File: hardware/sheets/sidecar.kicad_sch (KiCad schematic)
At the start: 3 parts, among them J1 Conn_02x32_Odd_Even

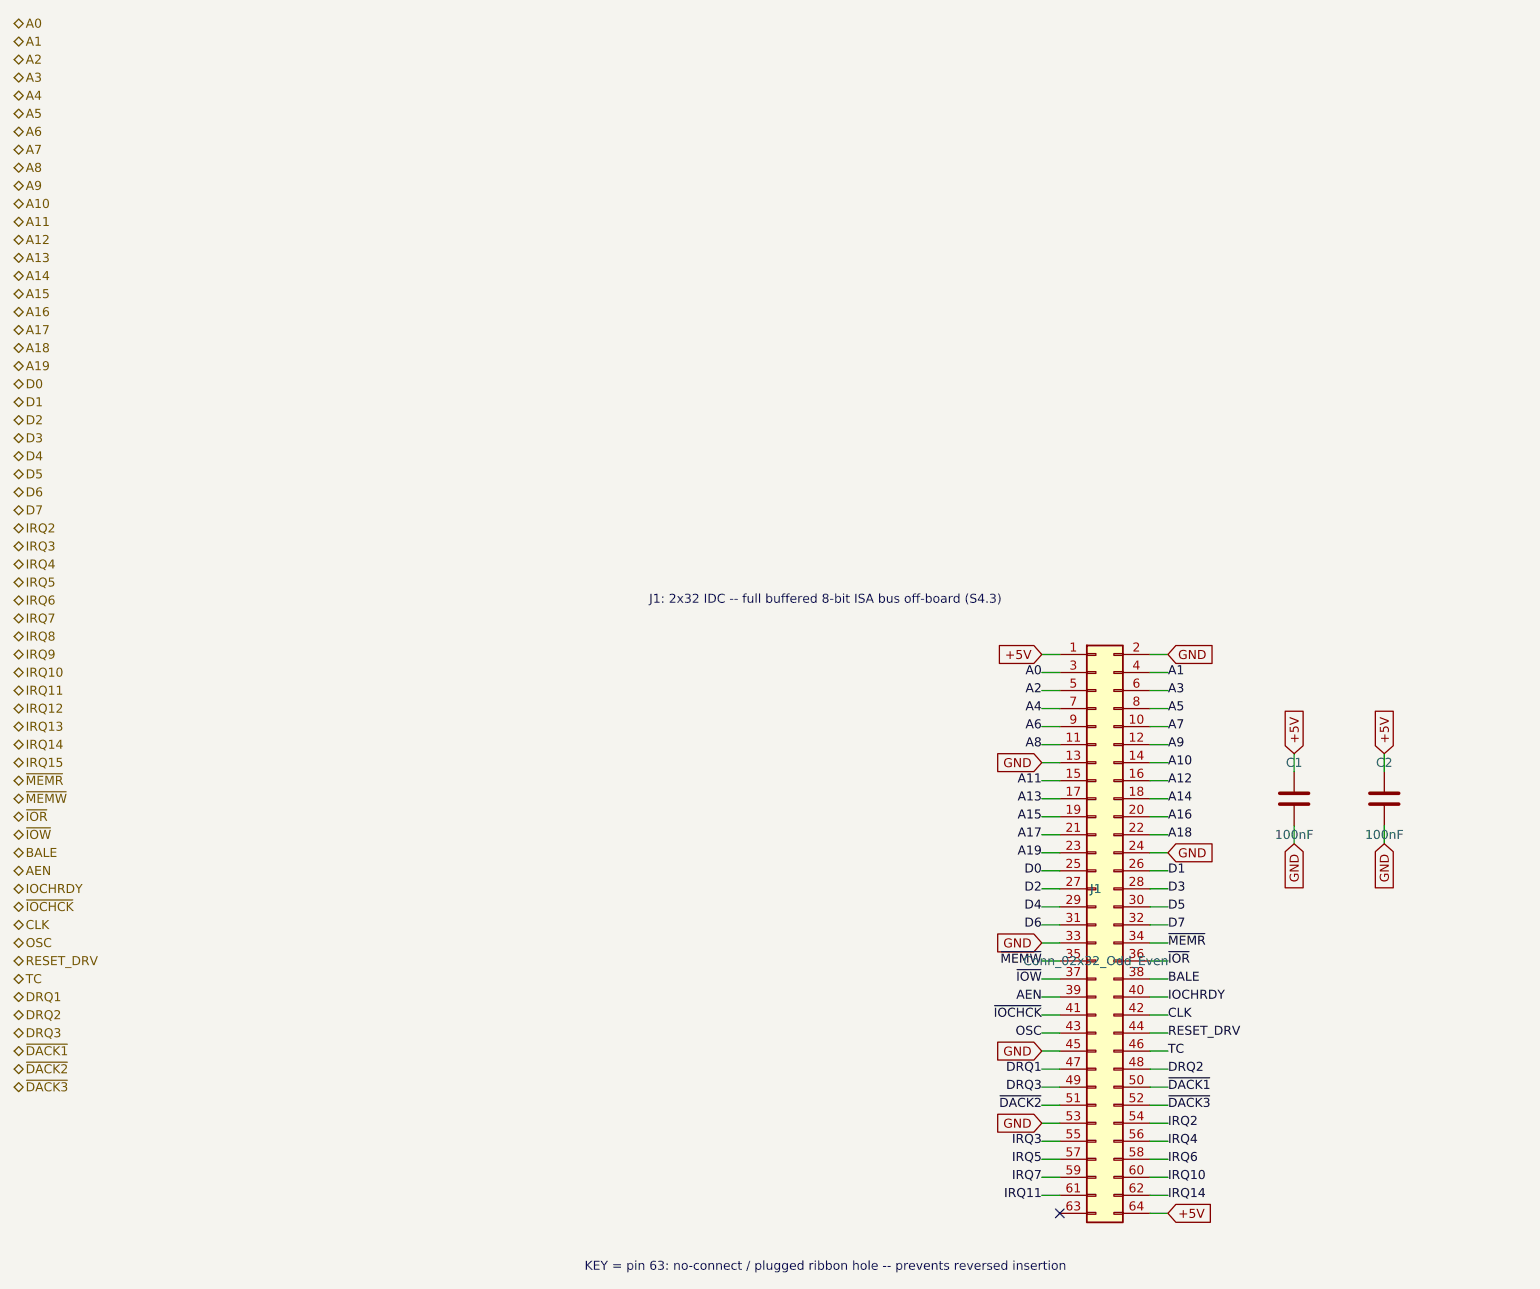
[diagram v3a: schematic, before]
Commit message: Add shared ISA connector + standalone chainable soft-card PCBs
isa_conn.py extracts the 2x32 ISA header into a reusable place_header() helper
(with per-card net remap + IRQ8 added); sidecar.py now uses it so the motherboard
edge and dev cards share one pinout. Each soft card (video/com/lpt/rtc/storage)
gets a standalone card_*.py PCB = the soft-card logic + two chainable ISA headers
(J_IN/J_OUT pass-through), built to hardware/cards/ as its own A2 top-level
project. Soft-card build() gains expose=False so cards tie to on-card headers
instead of a parent. Bus+power flow through the headers so cards daisy-chain for
development; the integrated motherboard is unchanged. Structural ERC=0 on all
cards; pass-through + logic taps verified in the netlists.

Co-Authored-By: Claude Opus 4.8 (1M context) <noreply@anthropic.com>
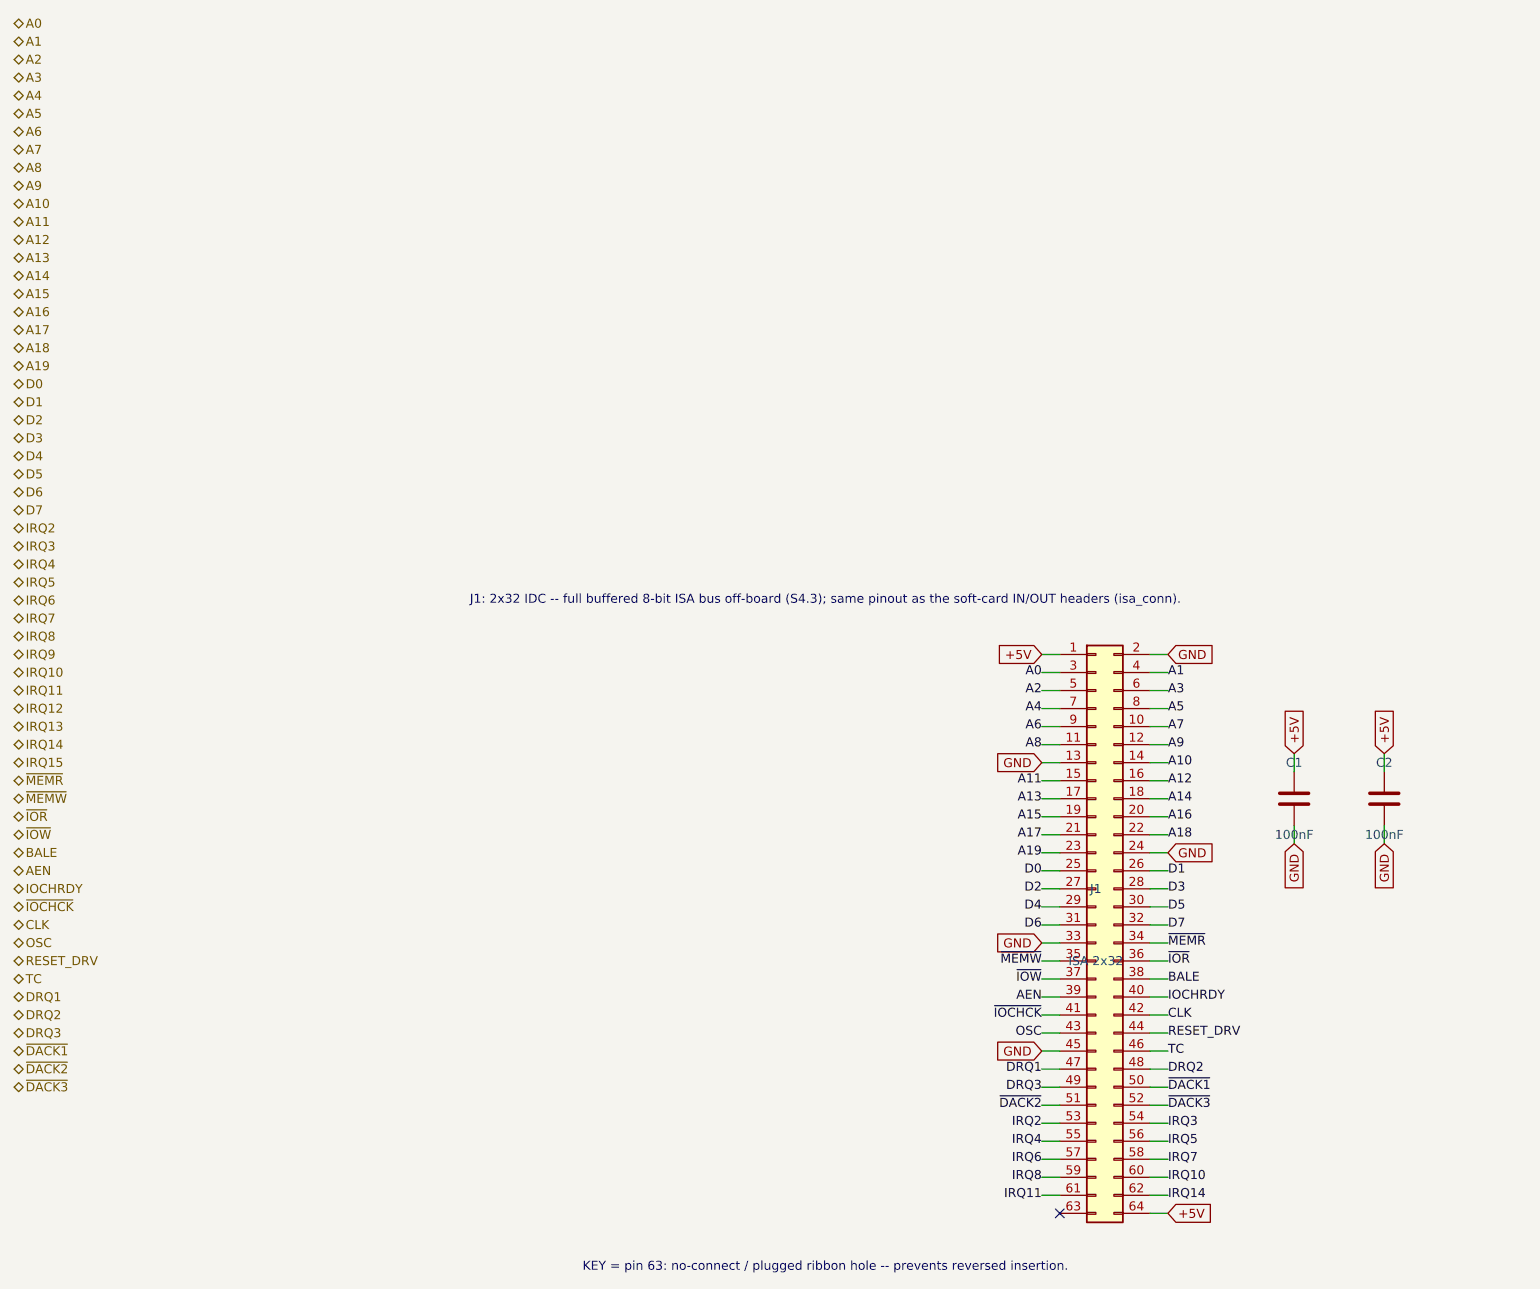
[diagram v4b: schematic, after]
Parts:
- J1: value Conn_02x32_Odd_Even -> ISA 2x32
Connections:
- net GND: no longer J1.53 (Pin_53)
- net IRQ2: now also J1.53 (Pin_53); no longer J1.54 (Pin_54)
- net IRQ3: now also J1.54 (Pin_54); no longer J1.55 (Pin_55)
- net IRQ4: now also J1.55 (Pin_55); no longer J1.56 (Pin_56)
- net IRQ5: now also J1.56 (Pin_56); no longer J1.57 (Pin_57)
- net IRQ6: now also J1.57 (Pin_57); no longer J1.58 (Pin_58)
- net IRQ7: now also J1.58 (Pin_58); no longer J1.59 (Pin_59)
- net IRQ8: now also J1.59 (Pin_59)
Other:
- note added: "J1: 2x32 IDC -- full buffered 8-bit ISA bus off-board (S4.3); same pinout as the soft-card IN/OUT headers (isa_conn)."
- note added: "KEY = pin 63: no-connect / plugged ribbon hole -- prevents reversed insertion."
- note removed: "J1: 2x32 IDC -- full buffered 8-bit ISA bus off-board (S4.3)"
- note removed: "KEY = pin 63: no-connect / plugged ribbon hole -- prevents reversed insertion"
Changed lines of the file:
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@@
 		)
 	)
-	(global_label "GND"
-		(shape input)
+	(label "IRQ2"
 		(at 170.18 180.34 180)
 		(effects
@@
 		)
 	)
-	(label "IRQ2"
+	(label "IRQ3"
 		(at 187.96 180.34 0)
 		(effects
@@
 		)
 	)
-	(label "IRQ3"
+	(label "IRQ4"
 		(at 170.18 182.88 180)
 		(effects
@@
 		)
 	)
-	(label "IRQ4"
+	(label "IRQ5"
 		(at 187.96 182.88 0)
 		(effects
@@
 		)
 	)
-	(label "IRQ5"
+	(label "IRQ6"
 		(at 170.18 185.42 180)
 		(effects
@@
 		)
 	)
-	(label "IRQ6"
+	(label "IRQ7"
 		(at 187.96 185.42 0)
 		(effects
@@
 		)
 	)
-	(label "IRQ7"
+	(label "IRQ8"
 		(at 170.18 187.96 180)
 		(effects
@@
 		)
 	)
-	(text "KEY = pin 63: no-connect / plugged ribbon hole -- prevents reversed insertion"
-		(at 139.7 200.66 0)
-		(effects
-			(font
-				(size 1.27 1.27)
-			)
-		)
-	)
-	(text "J1: 2x32 IDC -- full buffered 8-bit ISA bus off-board (S4.3)"
-		(at 139.7 106.68 0)
-		(effects
-			(font
-				(size 1.27 1.27)
-			)
-		)
-	)
 	(wire
 		(pts
@@
 		(shape input)
 		(at 218.44 140.97 270)
+		(effects
+			(font
+				(size 1.27 1.27)
+			)
+		)
+	)
+	(text "J1: 2x32 IDC -- full buffered 8-bit ISA bus off-board (S4.3); same pinout as the soft-card IN/OUT headers (isa_conn)."
+		(at 139.7 106.68 0)
+		(effects
+			(font
+				(size 1.27 1.27)
+			)
+		)
+	)
+	(text "KEY = pin 63: no-connect / plugged ribbon hole -- prevents reversed insertion."
+		(at 139.7 200.66 0)
 		(effects
 			(font
@@
 		(on_board yes)
 		(dnp no)
+		(fields_autoplaced yes)
 		(property "Reference" "J1"
 			(at 177.8 147.32 0)
@@
 			)
 		)
-		(property "Value" "Conn_02x32_Odd_Even"
+		(property "Value" "ISA 2x32"
 			(at 177.8 157.48 0)
 			(effects
@@
 		(instances
 			(project "mini-xt"
-				(path "/8479d0bf-d602-448f-b8c2-3cfe27dd8f32/3e94f2f0-56c8-4f92-8302-3d072f49a90e"
+				(path "/b06c1376-d75d-4e7b-982a-6cf2c80dfd97/7b218966-0463-42f1-811e-739393511f41"
 					(reference "J1201")
 					(unit 1)
@@
 		(on_board yes)
 		(dnp no)
+		(fields_autoplaced yes)
 		(property "Reference" "C1"
 			(at 205.74 129.54 0)
@@
 		(instances
 			(project "mini-xt"
-				(path "/8479d0bf-d602-448f-b8c2-3cfe27dd8f32/3e94f2f0-56c8-4f92-8302-3d072f49a90e"
+				(path "/b06c1376-d75d-4e7b-982a-6cf2c80dfd97/7b218966-0463-42f1-811e-739393511f41"
 					(reference "C1201")
 					(unit 1)
@@
 		(on_board yes)
 		(dnp no)
+		(fields_autoplaced yes)
 		(property "Reference" "C2"
 			(at 218.44 129.54 0)
@@
 		(instances
 			(project "mini-xt"
-				(path "/8479d0bf-d602-448f-b8c2-3cfe27dd8f32/3e94f2f0-56c8-4f92-8302-3d072f49a90e"
+				(path "/b06c1376-d75d-4e7b-982a-6cf2c80dfd97/7b218966-0463-42f1-811e-739393511f41"
 					(reference "C1202")
 					(unit 1)

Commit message: Re-base ISA connector on standard 8-bit ISA pinout (60-pin, PicoGUS-style)
isa_conn now uses the standard 8-bit ISA edge pinout on a 60-pin 2.54mm header
(Conn_02x30_Odd_Even), matching the PicoGUS Bus_ISA_8bit layout so the sidecar and
dev cards are pin-compatible with real ISA cards (and 60-pin ribbon is easy to
source). The unused ISA analog rails are reclaimed: pin7 -5V->~{IOCHCK}, pin11
-12V->GND (extra return), pin15 +12V->IRQ8; pin13 reserved/0WS# left NC. Drops the
non-standard IRQ10/11/14 (16-bit-extension signals on a real AT); DACK0/REFRESH#
now on its standard pin (undriven, for card compatibility). Change is confined to
isa_conn.py; sidecar + all card_* sheets inherit it. Verified pin map and
connectivity (IOCHCK->Bus MCU, IRQ8->collector+RTC); zero structural ERC on
motherboard and all five cards.

Co-Authored-By: Claude Opus 4.8 (1M context) <noreply@anthropic.com>
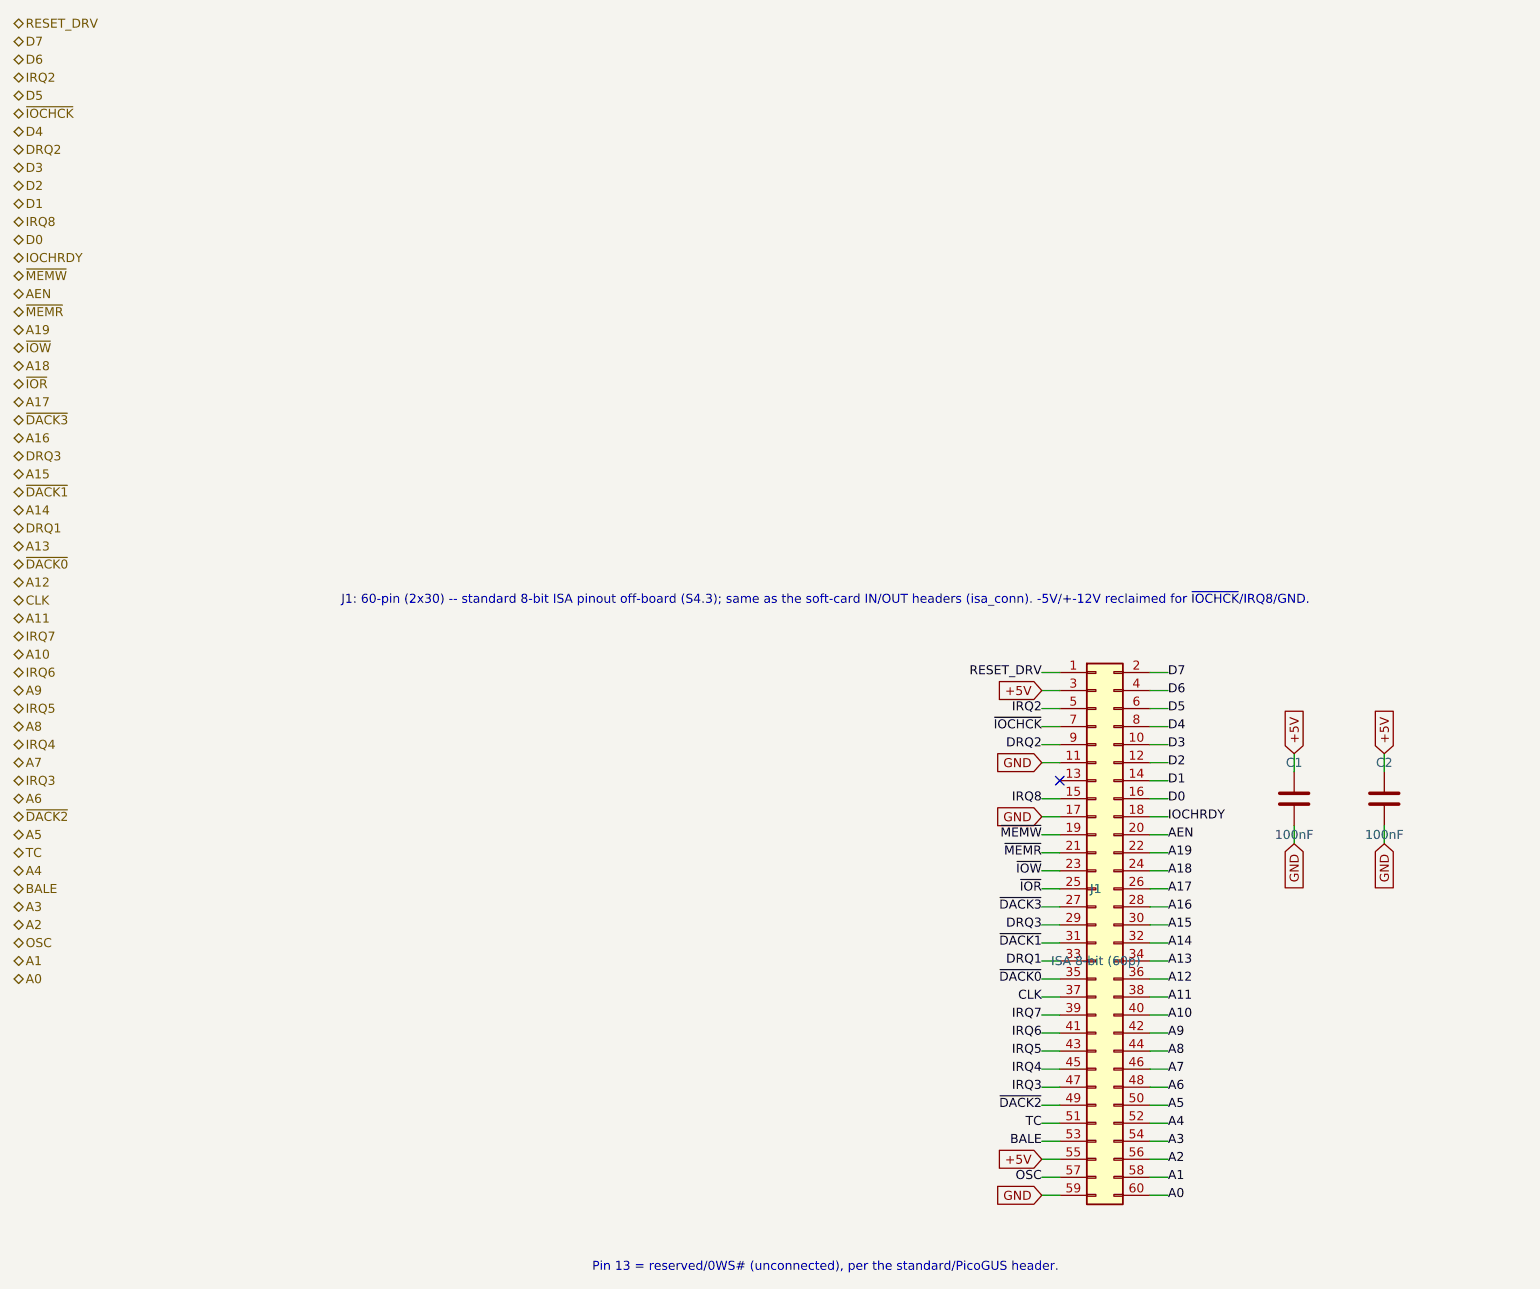
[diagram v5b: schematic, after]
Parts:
- removed J1: ISA 2x32, symbol Connector_Generic:Conn_02x32_Odd_Even
- added J1: ISA 8-bit (60p), symbol Connector_Generic:Conn_02x30_Odd_Even
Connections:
- net +5V: now also J1.3 (Pin_3), J1.55 (Pin_55)
- net A0: now also J1.60 (Pin_60)
- net A1: now also J1.58 (Pin_58)
- net A10: now also J1.40 (Pin_40)
- net A11: now also J1.38 (Pin_38)
- net A12: now also J1.36 (Pin_36)
- net A13: now also J1.34 (Pin_34)
- net A14: now also J1.32 (Pin_32)
- net A15: now also J1.30 (Pin_30)
- net A16: now also J1.28 (Pin_28)
- net A17: now also J1.26 (Pin_26)
- net A18: now also J1.24 (Pin_24)
- net A19: now also J1.22 (Pin_22)
- net A2: now also J1.56 (Pin_56)
- net A3: now also J1.54 (Pin_54)
- net A4: now also J1.52 (Pin_52)
- net A5: now also J1.50 (Pin_50)
- net A6: now also J1.48 (Pin_48)
- net A7: now also J1.46 (Pin_46)
- net A8: now also J1.44 (Pin_44)
- net A9: now also J1.42 (Pin_42)
- net AEN: now also J1.20 (Pin_20)
- net BALE: now also J1.53 (Pin_53)
- net CLK: now also J1.37 (Pin_37)
- net D0: now also J1.16 (Pin_16)
- net D1: now also J1.14 (Pin_14)
- net D2: now also J1.12 (Pin_12)
- net D3: now also J1.10 (Pin_10)
- net D4: now also J1.8 (Pin_8)
- net D5: now also J1.6 (Pin_6)
- net D6: now also J1.4 (Pin_4)
- net D7: now also J1.2 (Pin_2)
- net DRQ1: now also J1.33 (Pin_33)
- net DRQ2: now also J1.9 (Pin_9)
- net DRQ3: now also J1.29 (Pin_29)
- net GND: now also J1.11 (Pin_11), J1.17 (Pin_17), J1.59 (Pin_59)
- net IOCHRDY: now also J1.18 (Pin_18)
- net IRQ2: now also J1.5 (Pin_5)
- net IRQ3: now also J1.47 (Pin_47)
- net IRQ4: now also J1.45 (Pin_45)
- net IRQ5: now also J1.43 (Pin_43)
- net IRQ6: now also J1.41 (Pin_41)
- net IRQ7: now also J1.39 (Pin_39)
- net IRQ8: now also J1.15 (Pin_15)
- net OSC: now also J1.57 (Pin_57)
- net RESET_DRV: now also J1.1 (Pin_1)
- net TC: now also J1.51 (Pin_51)
- net ~{DACK1}: now also J1.31 (Pin_31)
- net ~{DACK2}: now also J1.49 (Pin_49)
- net ~{DACK3}: now also J1.27 (Pin_27)
- net ~{IOCHCK}: now also J1.7 (Pin_7)
- net ~{IOR}: now also J1.25 (Pin_25)
- net ~{IOW}: now also J1.23 (Pin_23)
- net ~{MEMR}: now also J1.21 (Pin_21)
- net ~{MEMW}: now also J1.19 (Pin_19)
- new net ~{DACK0}: J1.35 (Pin_35)
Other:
- note added: "J1: 60-pin (2x30) -- standard 8-bit ISA pinout off-board (S4.3); same as the soft-card IN/OUT headers (isa_conn). -5V/+-12V reclaimed for ~{IOCHCK}/IRQ8/GND."
- note added: "Pin 13 = reserved/0WS# (unconnected), per the standard/PicoGUS header."
- note removed: "J1: 2x32 IDC -- full buffered 8-bit ISA bus off-board (S4.3); same pinout as the soft-card IN/OUT headers (isa_conn)."
- note removed: "KEY = pin 63: no-connect / plugged ribbon hole -- prevents reversed insertion."
- title: Sidecar -- 2x32 IDC ISA expansion header -> Sidecar -- 60-pin (2x30) ISA expansion header
